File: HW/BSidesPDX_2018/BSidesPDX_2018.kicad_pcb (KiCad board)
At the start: 2 copper layers, 94.7 x 67.7 mm, 46 parts, among them J1 AVR-ISP-6, J2 USB_B_Micro, U1 ATTINY861-15XD, X1 Badgelife_shitty_connector, X2 Badgelife_shitty_connector, X3 Badgelife_shitty_connector, X4 Badgelife_shitty_connector

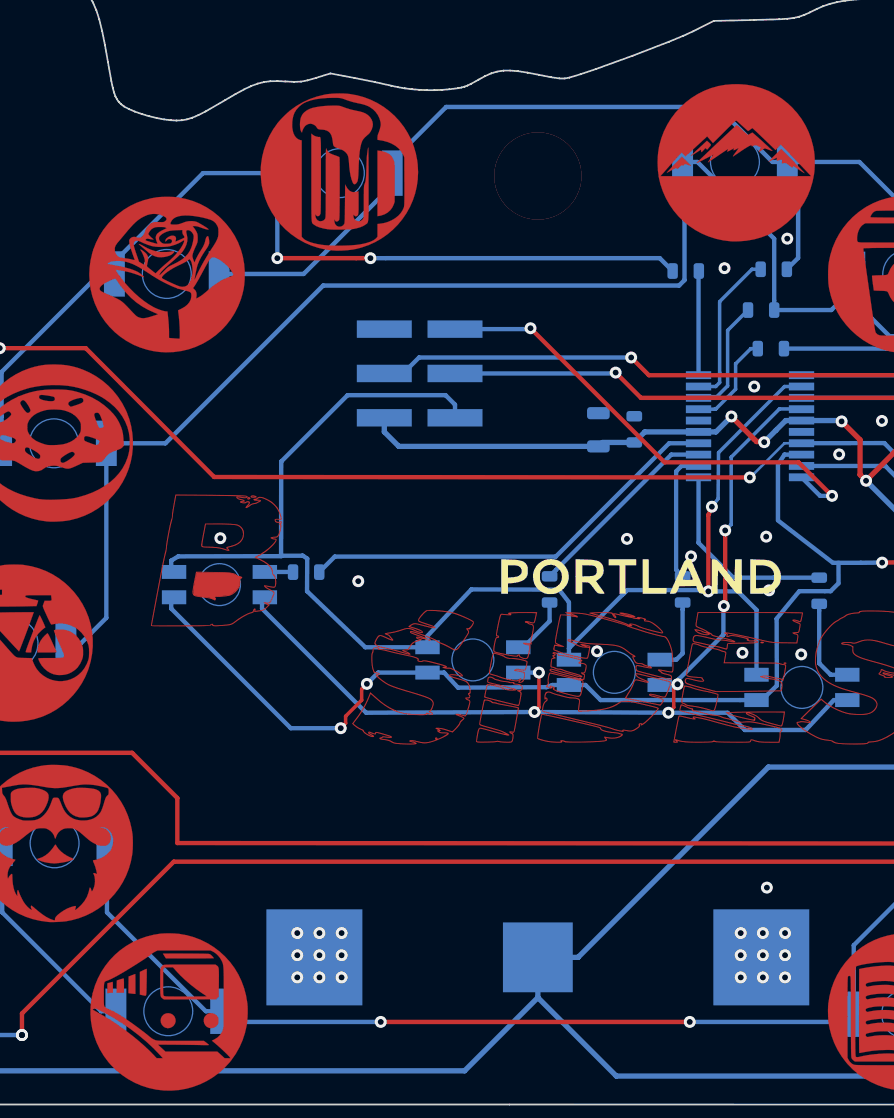
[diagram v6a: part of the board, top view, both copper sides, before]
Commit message: cleaned up USB schematic, changed USB resistor values. fixed shorted traces around LED apature
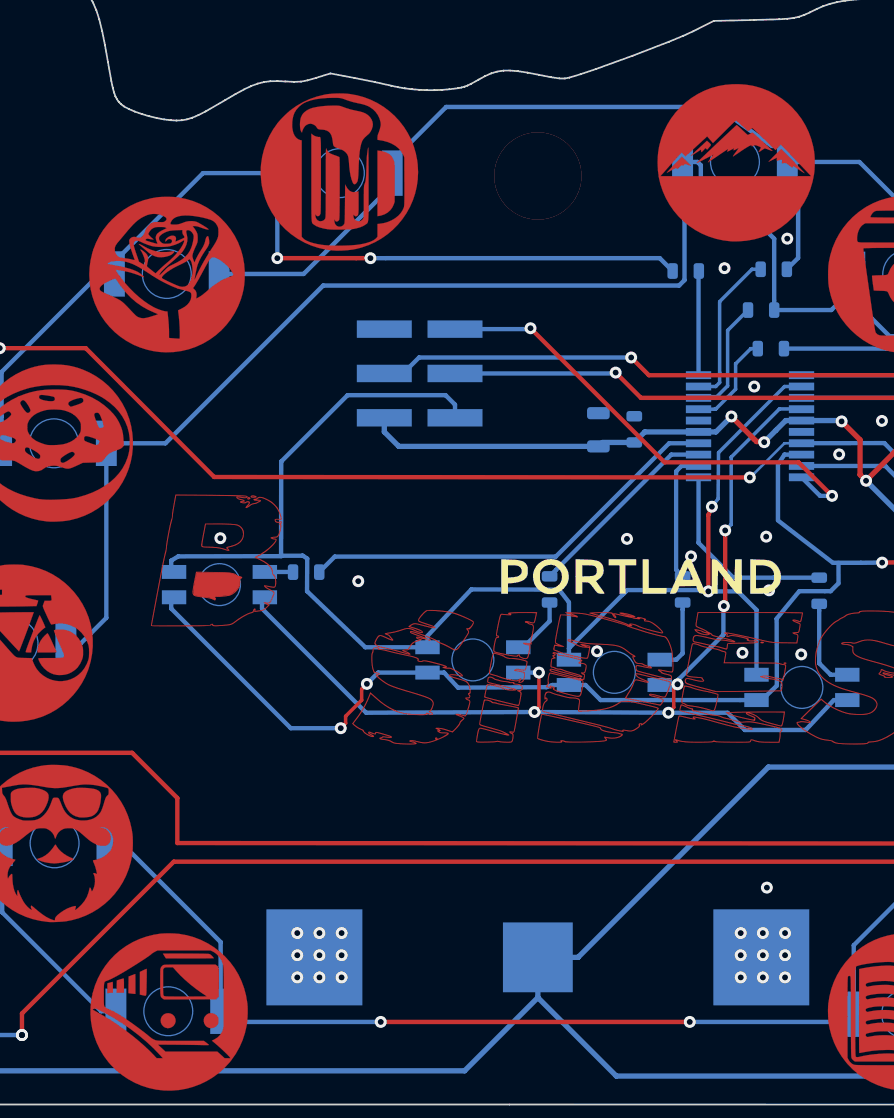
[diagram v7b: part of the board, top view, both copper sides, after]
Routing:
- net /ROW_3: track 106.1 -> 107.6 mm
- net /ROW_2: track 109.8 -> 109.2 mm
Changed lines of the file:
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@@
-(kicad_pcb (version 20171130) (host pcbnew 5.0.0-4.fc30)
+(kicad_pcb (version 20171130) (host pcbnew "(5.0.0)")
   (general
     (thickness 1.6)
     (drawings 412)
-    (tracks 562)
+    (tracks 565)
     (zones 0)
     (modules 46)
@@
   (page A4)
   (layers
-    (0 F.Cu signal)
+    (0 F.Cu signal hide)
     (31 B.Cu signal)
     (32 B.Adhes user)
@@
     (37 F.SilkS user)
     (38 B.Mask user)
-    (39 F.Mask user)
+    (39 F.Mask user hide)
     (40 Dwgs.User user)
     (41 Cmts.User user)
@@
     (46 B.CrtYd user)
     (47 F.CrtYd user)
-    (48 B.Fab user)
+    (48 B.Fab user hide)
     (49 F.Fab user)
   )
   (setup
-    (last_trace_width 0.1524)
+    (last_trace_width 0.254)
     (user_trace_width 0.2032)
     (user_trace_width 0.254)
@@
     (pad_to_mask_clearance 0.0508)
     (aux_axis_origin 0 0)
-    (visible_elements FFFFFF7F)
+    (visible_elements 7FFFFFFF)
     (pcbplotparams
       (layerselection 0x010f0_80000001)
@@
   (segment (start 130.14478 93.05544) (end 134.98244 93.05544) (width 0.254) (layer B.Cu) (net 7))
   (segment (start 140.0584 87.27948) (end 140.0584 86.57948) (width 0.25) (layer B.Cu) (net 7))
-  (segment (start 161.8398 86.6394) (end 158.6902 83.4898) (width 0.254) (layer B.Cu) (net 7))
-  (segment (start 140.0584 86.57948) (end 143.14808 83.4898) (width 0.254) (layer B.Cu) (net 7))
-  (segment (start 158.6902 83.4898) (end 143.14808 83.4898) (width 0.254) (layer B.Cu) (net 7))
-  (segment (start 162.6898 86.6394) (end 161.8398 86.6394) (width 0.25) (layer B.Cu) (net 7))
+  (segment (start 162.6898 85.725) (end 161.8398 85.725) (width 0.254) (layer B.Cu) (net 7))
   (segment (start 182.309201 116.7511) (end 182.309201 120.994399) (width 0.25) (layer B.Cu) (net 7))
   (segment (start 182.309201 120.994399) (end 179.0982 124.2054) (width 0.25) (layer B.Cu) (net 7))
@@
   (segment (start 163.309301 88.812901) (end 162.6898 88.1934) (width 0.254) (layer B.Cu) (net 7))
   (segment (start 162.663 92.7862) (end 163.309301 92.139899) (width 0.254) (layer B.Cu) (net 7))
+  (segment (start 143.14808 83.4898) (end 140.0584 86.57948) (width 0.254) (layer B.Cu) (net 7))
+  (segment (start 161.798 85.725) (end 158.6902 83.4898) (width 0.254) (layer B.Cu) (net 7))
+  (segment (start 158.6902 83.4898) (end 143.14808 83.4898) (width 0.254) (layer B.Cu) (net 7))
   (segment (start 157.6034 92.9048) (end 157.6204 92.8878) (width 0.25) (layer B.Cu) (net 8))
   (segment (start 157.6034 98.8528) (end 157.6034 92.9048) (width 0.25) (layer B.Cu) (net 8))
@@
   (segment (start 173.0855 112.8767) (end 174.5342 114.3254) (width 0.25) (layer B.Cu) (net 9))
   (segment (start 173.0855 102.8065) (end 173.0855 112.8767) (width 0.25) (layer B.Cu) (net 9))
-  (segment (start 123.71858 127.21904) (end 123.71858 125.66904) (width 0.25) (layer B.Cu) (net 9))
-  (segment (start 129.38114 135.28802) (end 123.71858 129.62546) (width 0.25) (layer B.Cu) (net 9))
-  (segment (start 123.71858 129.62546) (end 123.71858 127.21904) (width 0.25) (layer B.Cu) (net 9))
-  (segment (start 130.23114 135.28802) (end 129.38114 135.28802) (width 0.25) (layer B.Cu) (net 9))
   (segment (start 166.32402 135.28802) (end 166.4942 135.4582) (width 0.25) (layer B.Cu) (net 9))
   (segment (start 130.23114 135.9) (end 139.4 135.9) (width 0.254) (layer B.Cu) (net 9))
@@
   (segment (start 169.530202 97.3328) (end 173.0855 100.888098) (width 0.25) (layer B.Cu) (net 9))
   (segment (start 162.4965 97.3328) (end 169.530202 97.3328) (width 0.25) (layer B.Cu) (net 9))
+  (segment (start 124.57258 125.66904) (end 123.71858 125.66904) (width 0.254) (layer B.Cu) (net 9))
+  (segment (start 130.23114 131.3276) (end 124.57258 125.66904) (width 0.254) (layer B.Cu) (net 9))
+  (segment (start 130.23114 135.28802) (end 130.23114 131.3276) (width 0.254) (layer B.Cu) (net 9))
   (segment (start 181.3842 104.2552) (end 179.9355 102.8065) (width 0.25) (layer B.Cu) (net 10))
   (segment (start 179.9355 102.8065) (end 179.0855 102.8065) (width 0.25) (layer B.Cu) (net 10))
@@
   (segment (start 165.213 95.123) (end 166.5577 93.7783) (width 0.25) (layer B.Cu) (net 10))
   (segment (start 161.9384 95.123) (end 165.213 95.123) (width 0.25) (layer B.Cu) (net 10))
-  (segment (start 161.9384 94.573) (end 161.9384 95.123) (width 0.25) (layer B.Cu) (net 10))
-  (segment (start 161.9384 91.038) (end 161.9384 94.573) (width 0.25) (layer B.Cu) (net 10))
-  (segment (start 157.5398 86.6394) (end 161.9384 91.038) (width 0.25) (layer B.Cu) (net 10))
-  (segment (start 156.6898 86.6394) (end 157.5398 86.6394) (width 0.25) (layer B.Cu) (net 10))
   (segment (start 156.80141 88.30501) (end 156.6898 88.1934) (width 0.254) (layer B.Cu) (net 10))
   (segment (start 156.80141 93.407754) (end 156.80141 88.30501) (width 0.254) (layer B.Cu) (net 10))
@@
   (segment (start 179.0855 100.7646) (end 179.0855 102.8065) (width 0.254) (layer B.Cu) (net 10))
   (segment (start 174.9425 96.6216) (end 179.0855 100.7646) (width 0.254) (layer B.Cu) (net 10))
+  (segment (start 161.9384 94.573) (end 161.9384 95.123) (width 0.25) (layer B.Cu) (net 10))
+  (segment (start 161.9384 91.038) (end 161.9384 94.573) (width 0.254) (layer B.Cu) (net 10))
+  (segment (start 157.5438 86.6394) (end 157.734 86.8296) (width 0.254) (layer B.Cu) (net 10))
+  (segment (start 156.6898 86.6394) (end 157.5438 86.6394) (width 0.254) (layer B.Cu) (net 10))
+  (segment (start 157.734 86.8296) (end 157.734 89.408) (width 0.254) (layer B.Cu) (net 10))
+  (segment (start 157.734 89.408) (end 158.75 90.424) (width 0.254) (layer B.Cu) (net 10))
+  (segment (start 161.3244 90.424) (end 161.9384 91.038) (width 0.254) (layer B.Cu) (net 10))
+  (segment (start 158.75 90.424) (end 161.3244 90.424) (width 0.254) (layer B.Cu) (net 10))
   (segment (start 150.181 115.1498) (end 150.181 114.4998) (width 0.25) (layer B.Cu) (net 11))
   (segment (start 160.9252 116.0134) (end 160.9252 112.298998) (width 0.25) (layer B.Cu) (net 11))
@@
   (segment (start 165.6207 109.601) (end 165.62421 110.773558) (width 0.25) (layer B.Cu) (net 25))
   (segment (start 161.2252 117.4634) (end 160.9252 117.4634) (width 0.25) (layer B.Cu) (net 25))
-  (segment (start 162.0901 116.6368) (end 161.2252 117.4634) (width 0.25) (layer B.Cu) (net 25))
+  (segment (start 162.0901 116.6368) (end 161.2252 117.4634) (width 0.254) (layer B.Cu) (net 25))
   (segment (start 162.0774 112.8014) (end 162.0901 116.6368) (width 0.25) (layer B.Cu) (net 25))
   (segment (start 163.3728 111.2266) (end 162.0774 112.8014) (width 0.25) (layer B.Cu) (net 25))

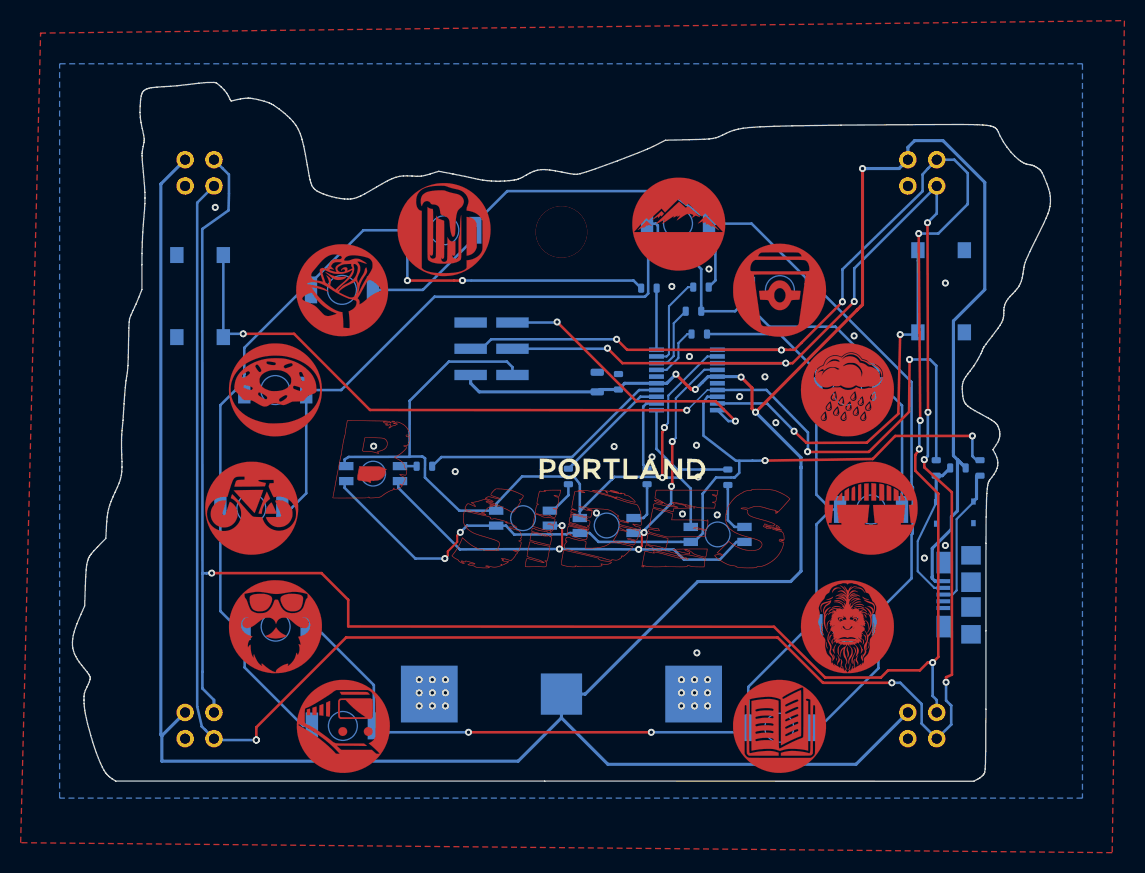
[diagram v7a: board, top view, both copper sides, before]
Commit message: fixed the battery foot print and updated the layout. Thickened the VCC traces. moved the SDA_MISO and SLC_SCK traces to make room for thick VCC trace. export new netlist for chages to USB block. Ran DRC and no errors. Have not checked for ground pours
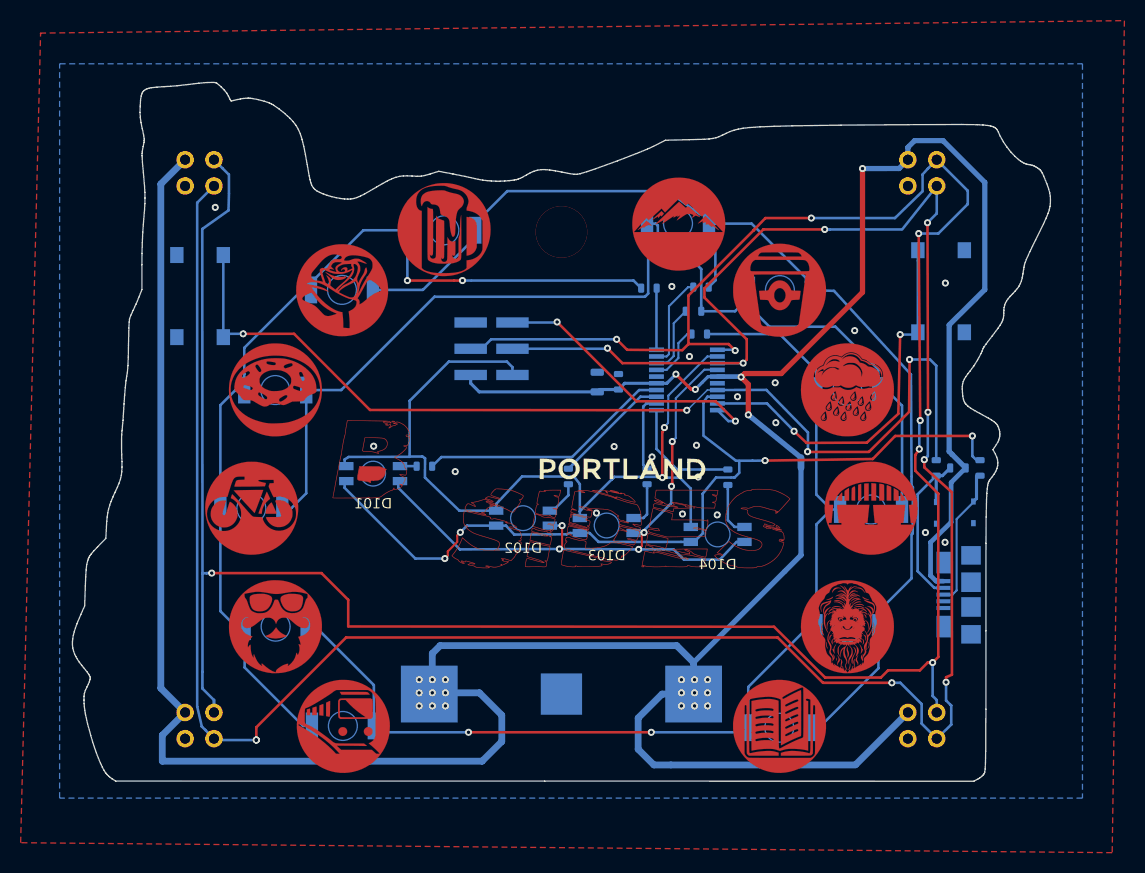
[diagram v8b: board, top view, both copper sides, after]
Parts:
- R5, R6: value 51R -> 68R
- R7: value 1K -> 1K5
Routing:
- net /3V0: track 309.1 -> 329.3 mm, vias 5 -> 23
- net /SCL_SCK: track 248.5 -> 252.6 mm
- net /D-: track 14.5 -> 17.4 mm
- net /ROW_2: track 109.2 -> 109.7 mm
- net /SDA_MOSI: track 255.8 -> 256.3 mm
- net GND: vias 39 -> 19
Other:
- net class Default: clearance 0.1524 -> 0.1778
- rule trace_clearance: 0.1524 -> 0.1778
